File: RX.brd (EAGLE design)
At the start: 160 x 100 mm, 61 parts, among them IC1 OPA354AIDBVR, IC2 LM7171BIN_NOPB, IC3 LTC6268IS6-10#TRMPBF, IC4 TPS72325DBVTG4, IC5 TLV75525PDBVR, IC6 TC7662BEOA, J4 455-1750-1-ND, U1 OPA656U, X1 BU-SMA-V

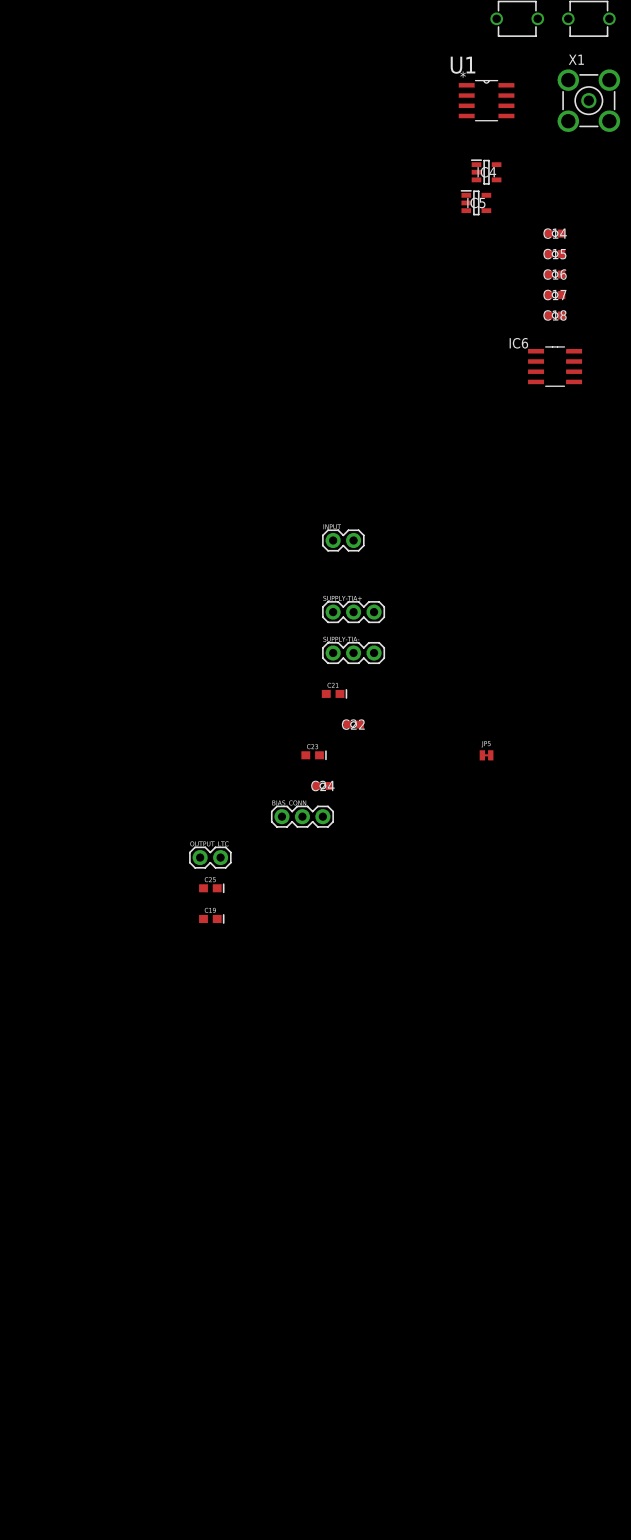
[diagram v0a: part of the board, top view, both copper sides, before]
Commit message: Menambahakan komponen komponen yang diperlukan untuk OPA656U kurang HPF untuk rangkaian OPA656U
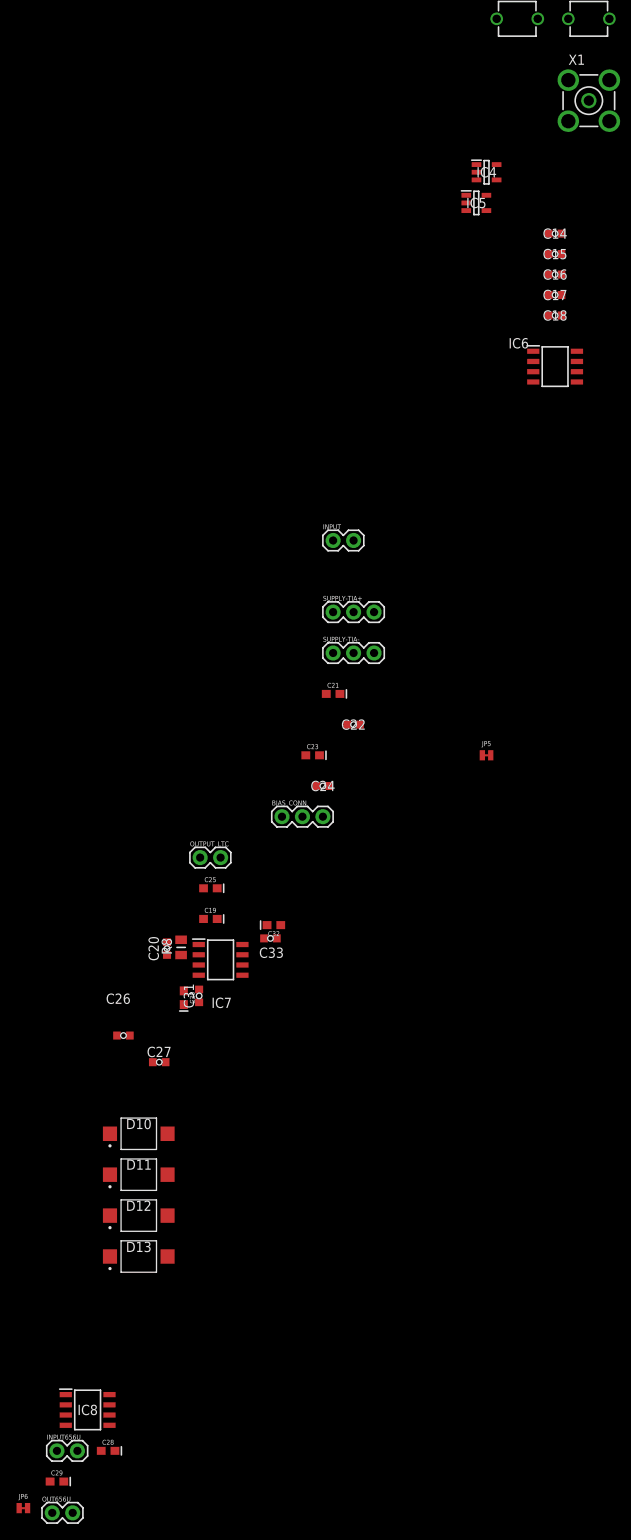
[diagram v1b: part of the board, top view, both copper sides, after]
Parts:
- removed U1: OPA656U, Texas Instruments_By_element14_Batch_1:SOIC127P600X175-8N
- added C20, C26, C27, C31, C33: 06033C104KAZ2A, SamacSys_Parts:CAPC1608X90N
- added C28, C29, C30, C32: 10uF, SparkFun-Capacitors:0603-POLAR
- added D10, D11, D12, D13: VBPW34SR, SamacSys_Parts:VBPW34SR
- added IC7: OPA656U, SamacSys_Parts:SOIC127P600X175-8N@1
- added IC8: TC7662BEOA, SamacSys_Parts:SOIC127P600X175-8N
- added INPUT656U, OUT656U: (no value), SparkFun-Connectors:1X02
- added JP6: JUMPER-SMT_2_NC_TRACE_NO-SILK, SparkFun-Jumpers:SMT-JUMPER_2_NC_TRACE_NO-SILK
- added R8: RG2012P-275-B-T5, SamacSys_Parts:RESC2012X50N
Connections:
- removed net +VS: U1.7
- removed net -VS: U1.4
- new net +V656U: C32.+, C33.2, IC7.7, IC8.8, INPUT656U.1
- new net -5VLTC: C14.2, C19.-, C23.-, C24.2, IC4.2, IC4.3, IC6.5
- new net -V656U: C29.-, C30.-, C31.2, IC7.4, IC8.5
- new net GND3: C26.1, C27.1, C29.+, C30.+, C31.1, C32.-, C33.1, IC7.3, IC8.3, INPUT656U.2, OUT656U.2
- new net N$15: C28.+, IC8.2
- new net N$17: C28.-, IC8.4
- new net N$2: C20.1, C26.2, C27.2, D10.2, D11.2, D12.2, D13.2, IC7.2, R8.1
- new net V_BIAS656U: D10.1, D11.1, D12.1, D13.1
- net -5V: no longer C14.2, C19.-, C23.-, C24.2, IC4.2, IC4.3, IC6.5
- net GND: no longer IC5.2
- net GND2: now also IC5.2
- net N$13: now also C20.2, IC7.6, JP6.1, OUT656U.1, R8.2; no longer D6.1, D7.1, D8.1, D9.1
- net V_BIAS: now also D6.1, D7.1, D8.1, D9.1
